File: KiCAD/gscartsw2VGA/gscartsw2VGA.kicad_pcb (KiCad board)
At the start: 2 copper layers, 51.1 x 30.8 mm, 5 parts, among them P1 VGA, P2 SCART_PAL

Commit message: Change PCB
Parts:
- JP1, JP2, JP3: footprint gscartsw2VGA:SolderJumper-3_P1.3mm_Open_RoundedPad1.0x1.5mm_NumberLabels -> Jumper:SolderJumper-3_P1.3mm_Open_RoundedPad1.0x1.5mm
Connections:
- P1 pad 4: (no net) -> Net-(P1-Pad4)
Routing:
- net Net-(P1-Pad4): track 0.00 -> 37.9 mm
- net /Sync: track 54.7 -> 53.5 mm, vias 1 -> 3
- net /Audio_L_Out: track 22.6 -> 23.5 mm

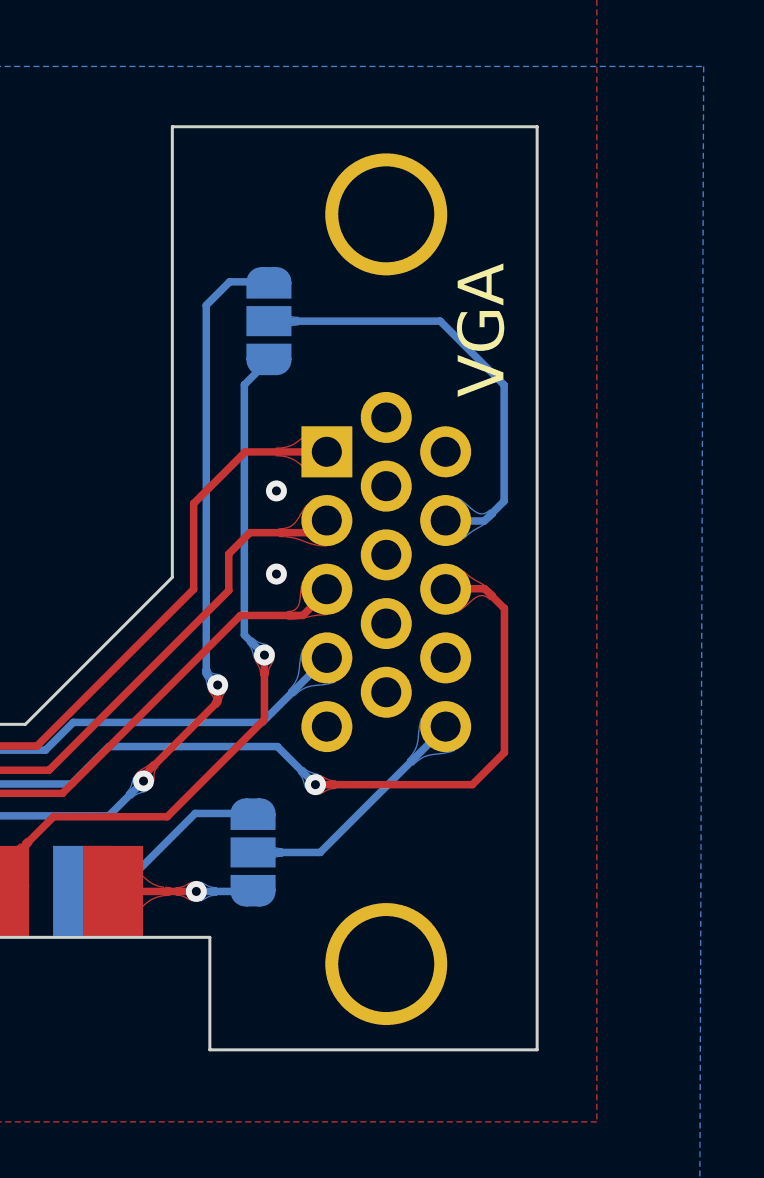
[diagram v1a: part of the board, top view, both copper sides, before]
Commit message: Add shielding grounding option
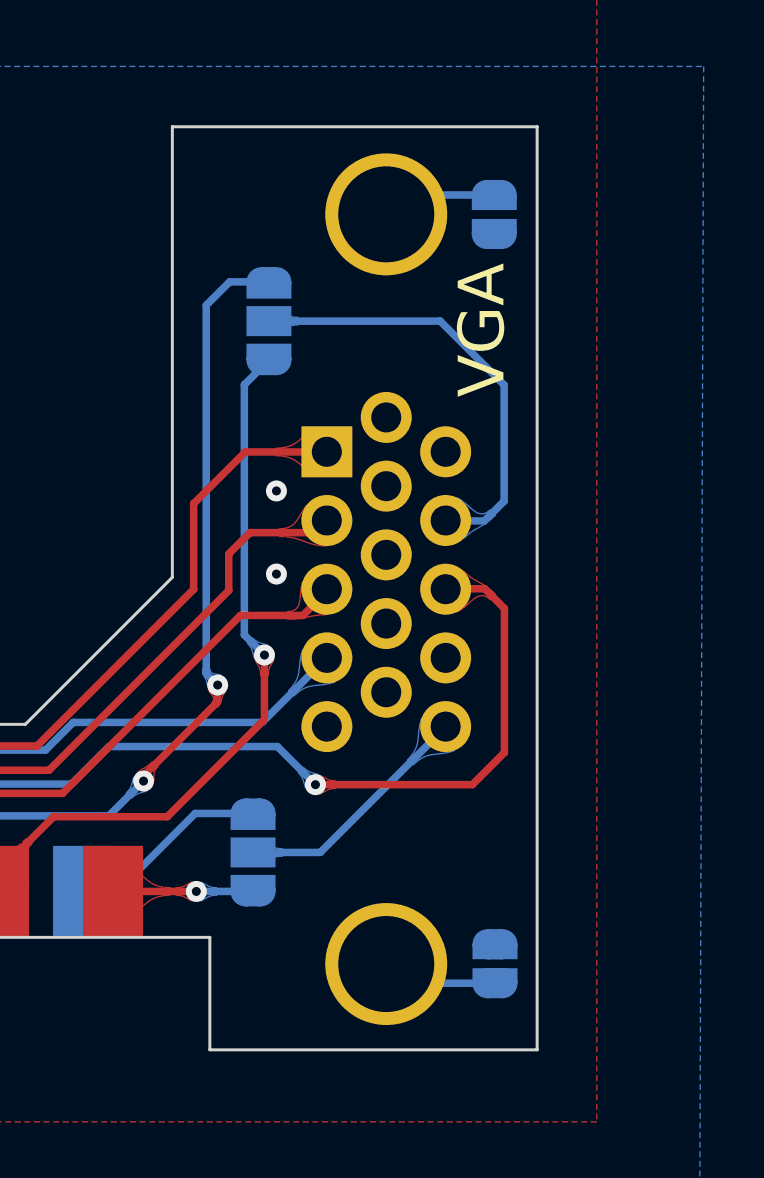
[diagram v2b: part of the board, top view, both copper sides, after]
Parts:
- added JP4: Shield Ground, Jumper:SolderJumper-2_P1.3mm_Open_RoundedPad1.0x1.5mm, B.Cu at (165.8, 106.2)
- added JP5: Shield Ground, Jumper:SolderJumper-2_P1.3mm_Open_RoundedPad1.0x1.5mm, B.Cu at (165.8, 81.3)
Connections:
- P1 pad 11: (no net) -> unconnected-(P1-Pad11)
- P1 pad 14: (no net) -> unconnected-(P1-Pad14)
- P1 pad 9: (no net) -> unconnected-(P1-Pad9)
- P1 pad S1: GND -> Net-(JP4-Pad1)
- P1 pad S2: GND -> Net-(JP5-Pad1)
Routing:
- net Net-(JP4-Pad1): track 0.00 -> 3.90 mm
- net Net-(JP5-Pad1): track 0.00 -> 3.87 mm
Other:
- net class Default removed
- board text added: "OUTPUT OPTION"

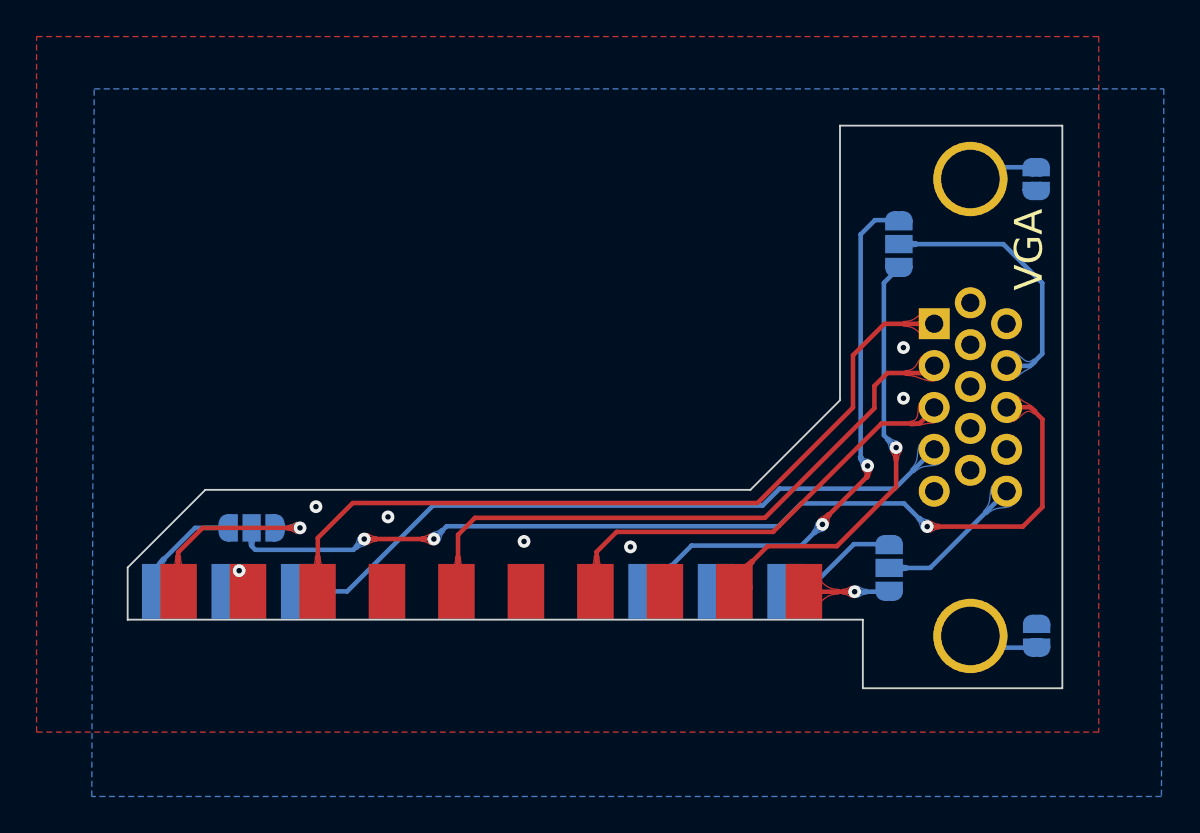
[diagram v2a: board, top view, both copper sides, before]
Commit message: Multiple Adjustments
- Add cable shielding grounding options
- Adjust 3D print details to allow for easier printing and assembly
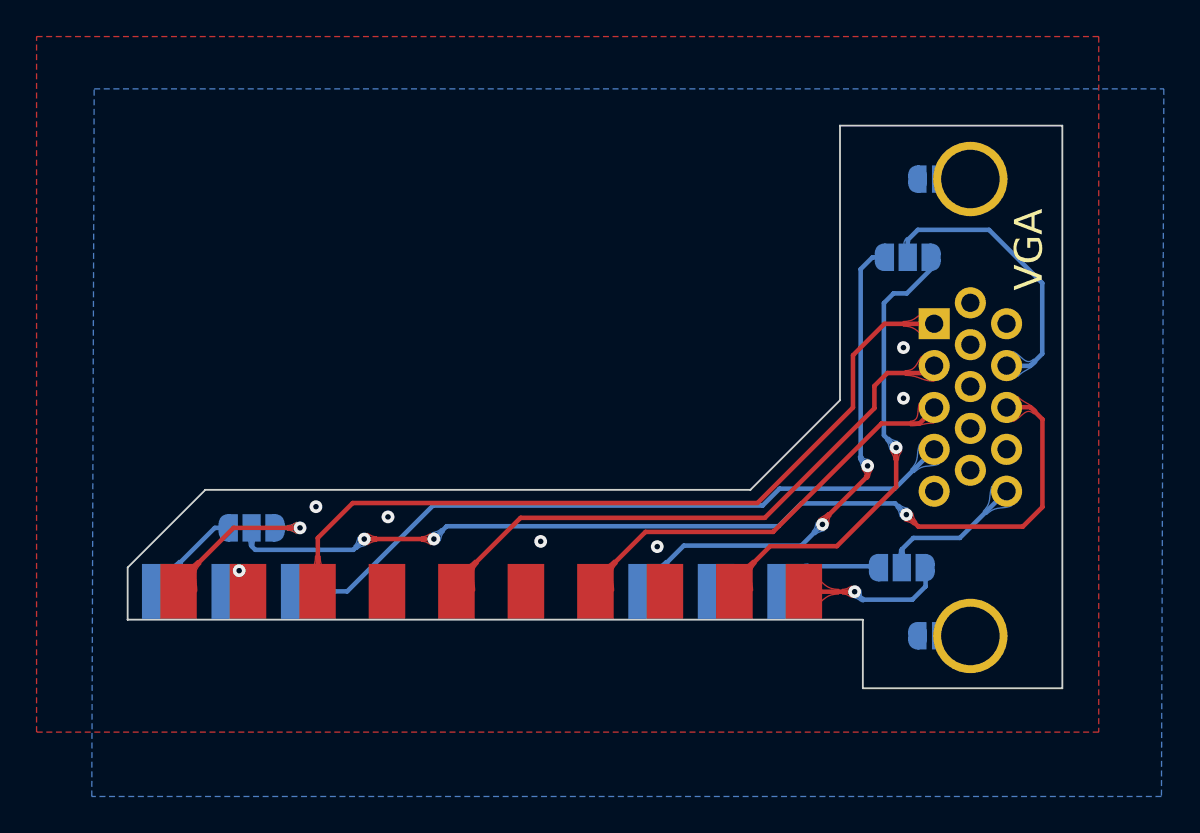
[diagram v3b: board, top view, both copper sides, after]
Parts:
- moved JP4 5.88 mm to (159.9, 106.2), turned to 180 degrees
- moved JP5 5.85 mm to (159.9, 81.3), turned to 180 degrees
- moved JP2 0.87 mm to (158.7, 85.5), turned to 180 degrees
- moved JP3 0.69 mm to (158.4, 102.5), turned to 180 degrees
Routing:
- net Net-(JP4-Pad1): track 3.90 -> 0.00 mm
- net Net-(JP5-Pad1): track 3.87 -> 0.00 mm
- net /Audio_R_Out: track 4.73 -> 8.23 mm
- net /Audio_L_In: track 30.6 -> 28.0 mm
- net /Audio_L_Out: track 23.5 -> 25.3 mm
- net /Green: track 33.5 -> 32.0 mm
- net /Audio_L_VGA: track 14.9 -> 15.9 mm
- net /CVBS_Out: track 10.7 -> 9.75 mm
- net /Blue: track 23.9 -> 23.0 mm
- net /Audio_R_In: track 6.78 -> 6.04 mm
- net /CVBS_In: track 6.14 -> 5.51 mm
